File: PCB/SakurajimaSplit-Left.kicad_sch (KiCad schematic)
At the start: 49 parts, among them J1 Conn_01x01_Pin, J10 Conn_01x01_Pin, J11 Conn_01x01_Pin, J12 Conn_01x01_Pin, J13 Conn_01x01_Pin, J14 Conn_01x01_Pin, J15 Conn_01x01_Pin, J16 Conn_01x01_Pin, J17 Conn_01x01_Pin, J18 Conn_01x01_Pin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

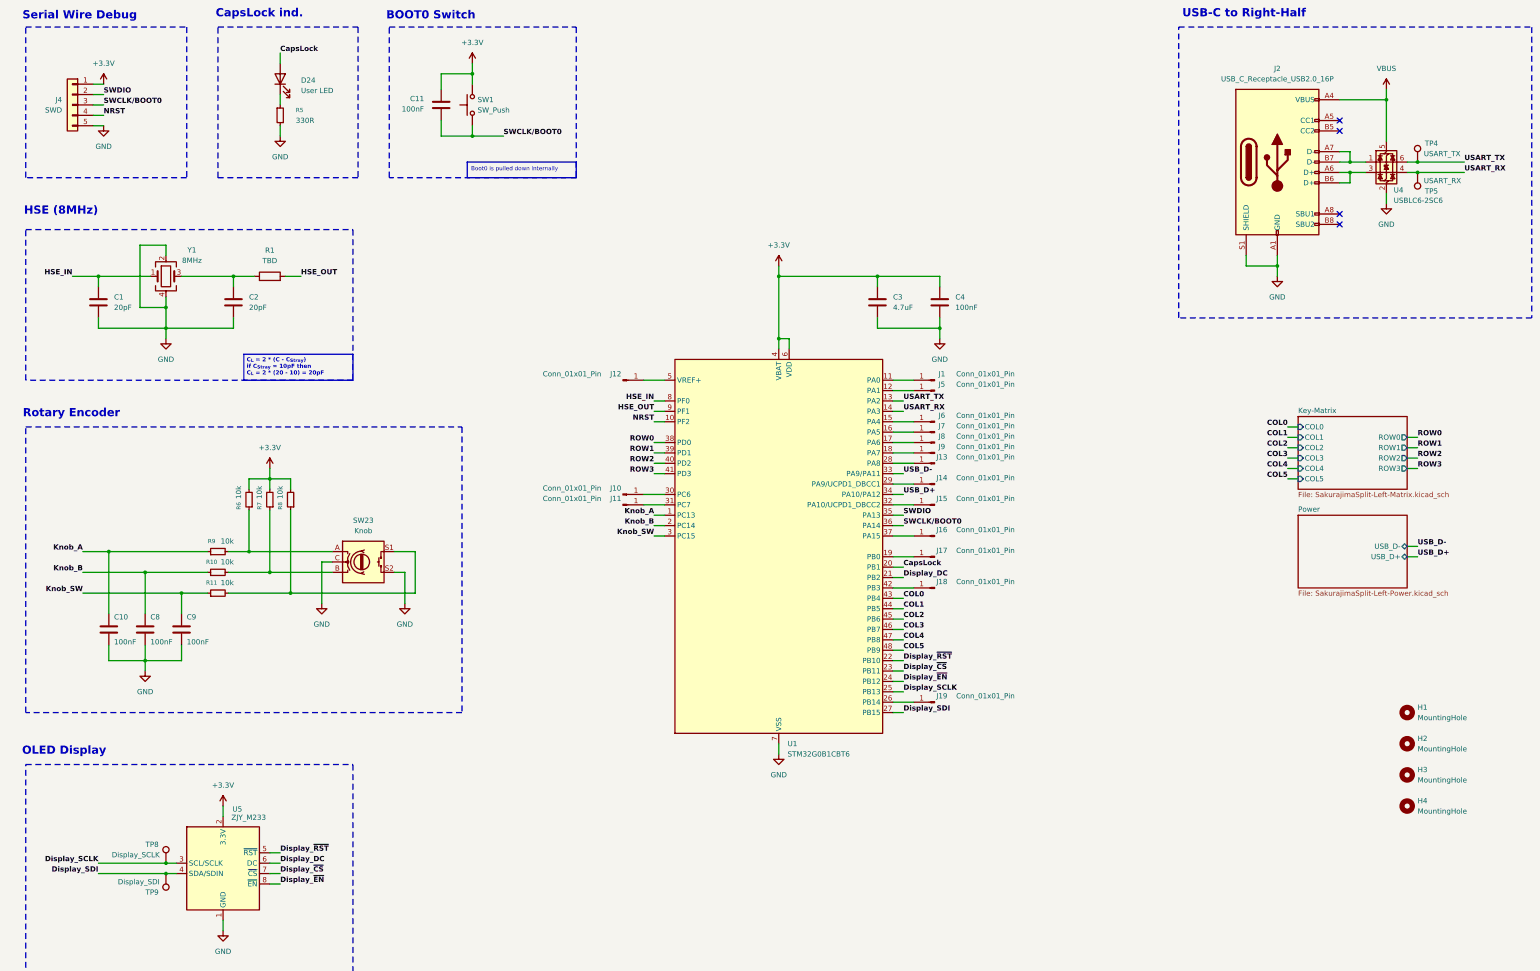
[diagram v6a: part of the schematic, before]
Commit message: feat(sch): cleanup and anotate schematic, choose components
- Fixed mistakes in schematic
- Anotated the schematic
- Found and chose components
- Added GND test points
- Ran ERC and fixed all errors and warnings
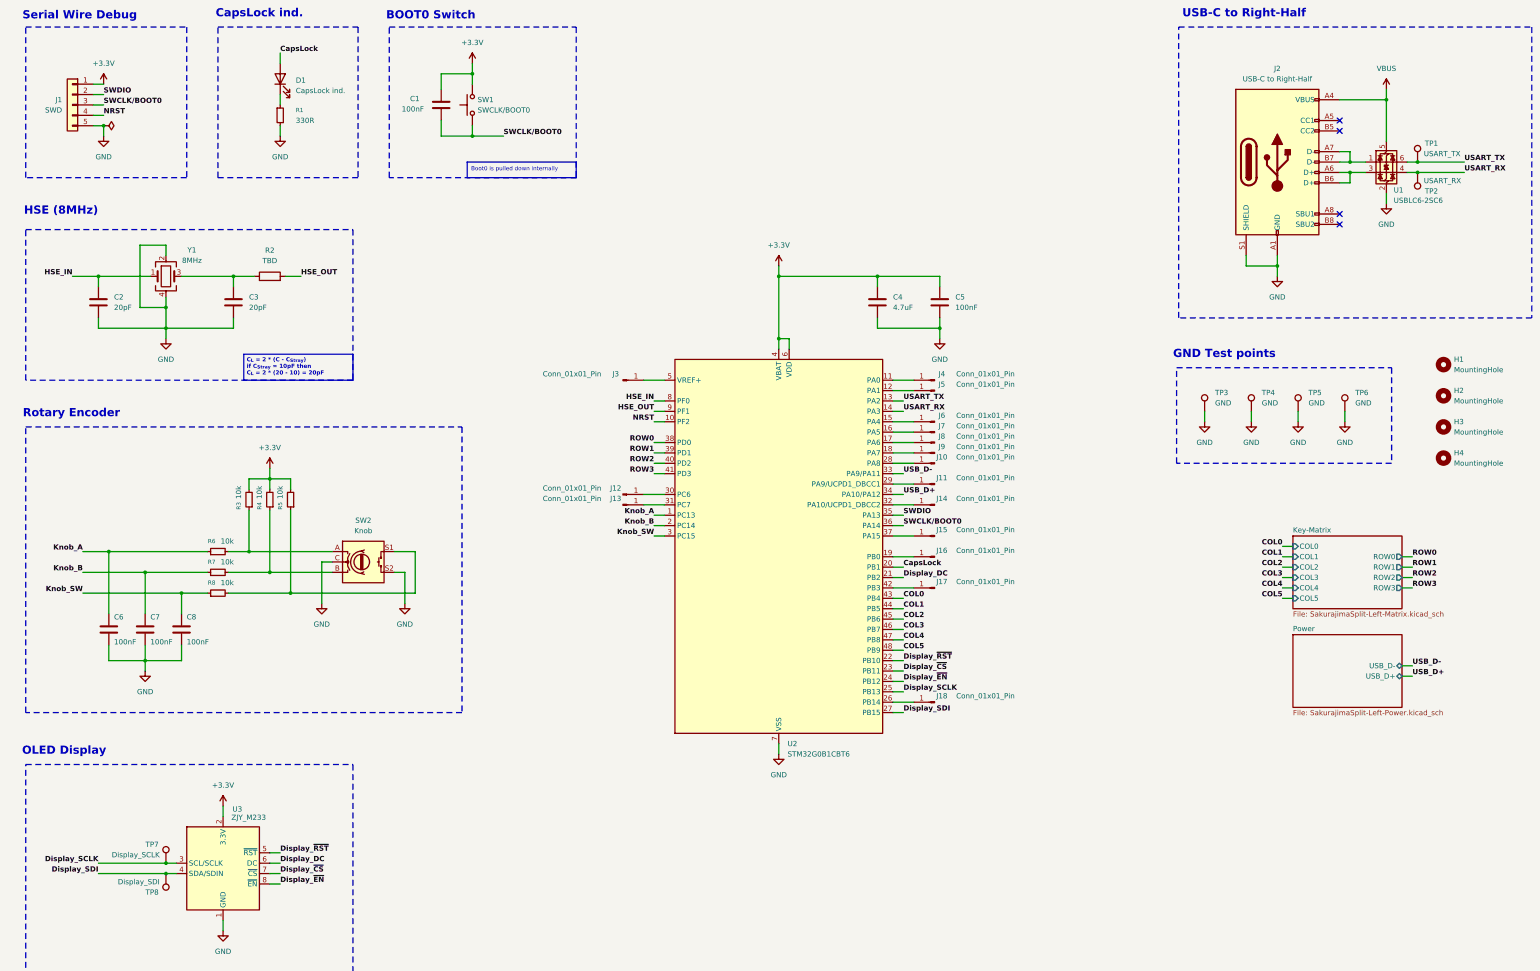
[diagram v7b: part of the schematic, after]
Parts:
- added TP3, TP4, TP5, TP6: GND, symbol Connector:TestPoint
- C1: renamed from C11; Distributor Link (none) -> https://lionelectronic.ir/products/4734-GRM188R72A104KA35D; Manufacturer (none) -> Murata; Manufacturer Part No. (none) -> GRM188R72A104KA35D
- C2: renamed from C1; Distributor Link (none) -> https://lionelectronic.ir/products/5170-GRM1555C1H220JA01D; Manufacturer (none) -> Murata; Manufacturer Part No. (none) -> GRM1555C1H220JA01D
- C3: renamed from C2; Distributor Link (none) -> https://lionelectronic.ir/products/5170-GRM1555C1H220JA01D; Manufacturer (none) -> Murata; Manufacturer Part No. (none) -> GRM1555C1H220JA01D
- C4: renamed from C3; Distributor Link (none) -> https://lionelectronic.ir/products/4714-GRM21BR61H475KE51L; Manufacturer (none) -> Murata; Manufacturer Part No. (none) -> GRM21BR61H475KE51L
- C5: renamed from C4; Distributor Link (none) -> https://lionelectronic.ir/products/4734-GRM188R72A104KA35D; Manufacturer (none) -> Murata; Manufacturer Part No. (none) -> GRM188R72A104KA35D
- C6: renamed from C10; Distributor Link (none) -> https://lionelectronic.ir/products/4734-GRM188R72A104KA35D; Manufacturer (none) -> Murata; Manufacturer Part No. (none) -> GRM188R72A104KA35D
- C7: renamed from C8; Distributor Link (none) -> https://lionelectronic.ir/products/4734-GRM188R72A104KA35D; Manufacturer (none) -> Murata; Manufacturer Part No. (none) -> GRM188R72A104KA35D
- C8: renamed from C9; Distributor Link (none) -> https://lionelectronic.ir/products/4734-GRM188R72A104KA35D; Manufacturer (none) -> Murata; Manufacturer Part No. (none) -> GRM188R72A104KA35D
- D1: renamed from D24; value User LED -> CapsLock ind.; Distributor Link (none) -> https://lionelectronic.ir/products/2215-XL-1608UWC-04; Manufacturer (none) -> XINGLIGHT; Manufacturer Part No. (none) -> XL-1608UWC-04
- H1, H2, H3, H4: Notes (none) -> M3 screws, Rubber o-rings
- J1: renamed from J4; Notes (none) -> 2.54mm right-angle pin header
- J10: renamed from J13; now left out of the parts list
- J11: renamed from J14; now left out of the parts list
- J12: renamed from J10; now left out of the parts list
- J13: renamed from J11; now left out of the parts list
- J14: renamed from J15; now left out of the parts list
- J15: renamed from J16; now left out of the parts list
- J16: renamed from J17; now left out of the parts list
- J17: renamed from J18; now left out of the parts list
- J18: renamed from J19; now left out of the parts list
- J2: value USB_C_Receptacle_USB2.0_16P -> USB-C to Right-Half; Distributor Link (none) -> https://lionelectronic.ir/products/3242-GT-USB-7010ASV; Manufacturer (none) -> G-Switch; Manufacturer Part No. (none) -> GT-USB-7010ASV
- J3: renamed from J12; now left out of the parts list
- J4: renamed from J1; now left out of the parts list
- J5, J6, J7, J8, J9: now left out of the parts list
- R1: renamed from R5; Distributor Link (none) -> https://lionelectronic.ir/products/1182-SER0603F330R; Manufacturer (none) -> VO Sub Brand (ER); Manufacturer Part No. (none) -> SER0603F330R
- R2: renamed from R1; Notes (none) -> Should be around 1k but 220R was also okay
- R3: renamed from R6; Distributor Link (none) -> https://lionelectronic.ir/products/1219-CR0603FA1002G; Manufacturer (none) -> LIZ Electronics; Manufacturer Part No. (none) -> CR0603FA1002G
- R4: renamed from R7; Distributor Link (none) -> https://lionelectronic.ir/products/1219-CR0603FA1002G; Manufacturer (none) -> LIZ Electronics; Manufacturer Part No. (none) -> CR0603FA1002G
- R5: renamed from R8; Distributor Link (none) -> https://lionelectronic.ir/products/1219-CR0603FA1002G; Manufacturer (none) -> LIZ Electronics; Manufacturer Part No. (none) -> CR0603FA1002G
- R6: renamed from R9; Distributor Link (none) -> https://lionelectronic.ir/products/1219-CR0603FA1002G; Manufacturer (none) -> LIZ Electronics; Manufacturer Part No. (none) -> CR0603FA1002G
- R7: renamed from R10; Distributor Link (none) -> https://lionelectronic.ir/products/1219-CR0603FA1002G; Manufacturer (none) -> LIZ Electronics; Manufacturer Part No. (none) -> CR0603FA1002G
- R8: renamed from R11; Distributor Link (none) -> https://lionelectronic.ir/products/1219-CR0603FA1002G; Manufacturer (none) -> LIZ Electronics; Manufacturer Part No. (none) -> CR0603FA1002G
- SW1: value SW_Push -> SWCLK/BOOT0; Distributor Link (none) -> https://lionelectronic.ir/products/5092-TS-1187A-B-A-B; Manufacturer (none) -> XKB Connection; Manufacturer Part No. (none) -> TS-1187A-B-A-B
- SW2: renamed from SW23; Distributor Link (none) -> https://lionelectronic.ir/products/2497-EC11L1525E05; Manufacturer (none) -> ALPSALPINE; Manufacturer Part No. (none) -> EC11L1525E05; Notes (none) -> Make sure height is okay
- TP1: renamed from TP4; now left out of the parts list
- TP2: renamed from TP5; now left out of the parts list
- TP7: renamed from TP8; now left out of the parts list
- TP8: renamed from TP9; now left out of the parts list
- U1: renamed from U4; Distributor Link (none) -> https://lionelectronic.ir/products/4780-USBLC6-4SC6; Manufacturer (none) -> STMicroelectronics; Manufacturer Part No. (none) -> USBLC6-4SC6
- U2: renamed from U1; Distributor Link (none) -> https://lionelectronic.ir/products/2851-STM32G0B1CBT6; Manufacturer (none) -> STMicroelectronics; Manufacturer Part No. (none) -> STM32G0B1CBT6
- U3: renamed from U5; Distributor Link (none) -> https://thecaferobot.com/store/2-23-inch-spi-iic-oled-displ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; Notes (none) -> Also need spacers
- Y1: Distributor Link (none) -> https://lionelectronic.ir/products/4281-X32258MSB4SI; Manufacturer (none) -> YXC; Manufacturer Part No. (none) -> X32258MSB4SI
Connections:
- net GND: now also TP3.1, TP4.1, TP5.1, TP6.1
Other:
- note added: "GND Test points"
- moved on the sheet: H1, H2, H3, H4

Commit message: feat(pcb): assign all footprints
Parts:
- C1, C5, C6, C7, C8: footprint (none) -> Capacitor_SMD:C_0603_1608Metric
- C2, C3: footprint (none) -> Capacitor_SMD:C_0402_1005Metric_Pad0.74x0.62mm_HandSolder
- C4: footprint (none) -> Capacitor_SMD:C_0805_2012Metric
- D1: footprint (none) -> LED_SMD:LED_0603_1608Metric
- H1, H2, H3, H4: footprint (none) -> MountingHole:MountingHole_3.2mm_M3_Pad
- J1: footprint (none) -> Connector_PinHeader_2.54mm:PinHeader_1x05_P2.54mm_Horizontal
- J10, J11, J12, J13, J14, J15, J16, J17, J18, J3, J4, J6, J7, J8, J9: footprint (none) -> Connector_Wire:SolderWirePad_1x01_SMD_1x2mm
- J2: footprint (none) -> Connector_USB:USB_C_Receptacle_G-Switch_GT-USB-7010ASV
- R1, R2, R3, R4, R5, R6, R7, R8: footprint (none) -> Resistor_SMD:R_0603_1608Metric
- SW1: footprint (none) -> Button_Switch_SMD:SW_Push_1P1T_XKB_TS-1187A
- SW2: footprint (none) -> Rotary_Encoder:RotaryEncoder_Alps_EC11E-Switch_Vertical_H20mm
- TP1, TP2, TP3, TP4, TP5, TP6, TP7, TP8: footprint (none) -> TestPoint:TestPoint_Pad_2.0x2.0mm
- Y1: footprint (none) -> Crystal:Crystal_SMD_3225-4Pin_3.2x2.5mm_HandSoldering
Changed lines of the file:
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@@
 			)
 		)
-		(property "Footprint" ""
+		(property "Footprint" "Rotary_Encoder:RotaryEncoder_Alps_EC11E-Switch_Vertical_H20mm"
 			(at 104.14 154.686 0)
 			(effects
@@
 			)
 		)
-		(property "Footprint" ""
+		(property "Footprint" "MountingHole:MountingHole_3.2mm_M3_Pad"
 			(at 372.11 118.11 0)
 			(effects
@@
 			)
 		)
-		(property "Footprint" ""
+		(property "Footprint" "Connector_Wire:SolderWirePad_1x01_SMD_1x2mm"
 			(at 247.65 165.1 0)
 			(effects
@@
 		(dnp no)
 		(fields_autoplaced yes)
-		(property "Reference" "#FLG04"
+		(property "Reference" "#FLG01"
 			(at 46.355 52.07 0)
 			(effects
@@
 			(project "SakurajimaSplit"
 				(path "/2049b6de-7453-46e1-ab60-70116abff9d6/d08add9a-e5d5-49be-809e-a90adb11436d"
-					(reference "#FLG04")
+					(reference "#FLG01")
 					(unit 1)
 				)
@@
 			)
 		)
-		(property "Footprint" ""
+		(property "Footprint" "Resistor_SMD:R_0603_1608Metric"
 			(at 72.39 161.29 0)
 			(effects
@@
 			)
 		)
-		(property "Footprint" ""
+		(property "Footprint" "Connector_Wire:SolderWirePad_1x01_SMD_1x2mm"
 			(at 247.65 157.48 0)
 			(effects
@@
 			)
 		)
-		(property "Footprint" ""
+		(property "Footprint" "Resistor_SMD:R_0603_1608Metric"
 			(at 72.39 156.21 0)
 			(effects
@@
 			)
 		)
-		(property "Footprint" ""
+		(property "Footprint" "Capacitor_SMD:C_0603_1608Metric"
 			(at 55.5752 179.07 0)
 			(effects
@@
 			)
 		)
-		(property "Footprint" ""
+		(property "Footprint" "Connector_Wire:SolderWirePad_1x01_SMD_1x2mm"
 			(at 171.45 142.24 0)
 			(effects
@@
 			)
 		)
-		(property "Footprint" ""
+		(property "Footprint" "Capacitor_SMD:C_0603_1608Metric"
 			(at 64.4652 179.07 0)
 			(effects
@@
 			)
 		)
-		(property "Footprint" ""
+		(property "Footprint" "Connector_Wire:SolderWirePad_1x01_SMD_1x2mm"
 			(at 247.65 129.54 0)
 			(effects
@@
 			)
 		)
-		(property "Footprint" ""
+		(property "Footprint" "Capacitor_SMD:C_0603_1608Metric"
 			(at 46.6852 179.07 0)
 			(effects
@@
 			)
 		)
-		(property "Footprint" ""
+		(property "Footprint" "TestPoint:TestPoint_Pad_2.0x2.0mm"
 			(at 370.84 60.96 0)
 			(effects
@@
 			)
 		)
-		(property "Footprint" ""
+		(property "Footprint" "Connector_Wire:SolderWirePad_1x01_SMD_1x2mm"
 			(at 247.65 139.7 0)
 			(effects
@@
 			)
 		)
-		(property "Footprint" ""
+		(property "Footprint" "Capacitor_SMD:C_0603_1608Metric"
 			(at 127.9652 50.8 0)
 			(effects
@@
 			)
 		)
-		(property "Footprint" ""
+		(property "Footprint" "Resistor_SMD:R_0603_1608Metric"
 			(at 90.17 143.51 0)
 			(effects
@@
 			)
 		)
-		(property "Footprint" ""
+		(property "Footprint" "Connector_Wire:SolderWirePad_1x01_SMD_1x2mm"
 			(at 247.65 193.04 0)
 			(effects
@@
 			)
 		)
-		(property "Footprint" ""
+		(property "Footprint" "Capacitor_SMD:C_0805_2012Metric"
 			(at 234.6452 99.06 0)
 			(effects
@@
 			)
 		)
-		(property "Footprint" ""
+		(property "Footprint" "Crystal:Crystal_SMD_3225-4Pin_3.2x2.5mm_HandSoldering"
 			(at 59.69 88.9 0)
 			(effects
@@
 			)
 		)
-		(property "Footprint" ""
+		(property "Footprint" "Capacitor_SMD:C_0603_1608Metric"
 			(at 249.8852 99.06 0)
 			(effects
@@
 			)
 		)
-		(property "Footprint" ""
+		(property "Footprint" "MountingHole:MountingHole_3.2mm_M3_Pad"
 			(at 372.11 110.49 0)
 			(effects
@@
 			)
 		)
-		(property "Footprint" ""
+		(property "Footprint" "Connector_Wire:SolderWirePad_1x01_SMD_1x2mm"
 			(at 247.65 124.46 0)
 			(effects
@@
 			)
 		)
-		(property "Footprint" ""
+		(property "Footprint" "Connector_Wire:SolderWirePad_1x01_SMD_1x2mm"
 			(at 171.45 144.78 0)
 			(effects
@@
 			)
 		)
-		(property "Footprint" ""
+		(property "Footprint" "TestPoint:TestPoint_Pad_2.0x2.0mm"
 			(at 318.77 121.92 0)
 			(effects
@@
 			)
 		)
-		(property "Footprint" ""
+		(property "Footprint" "Connector_PinHeader_2.54mm:PinHeader_1x05_P2.54mm_Horizontal"
 			(at 36.83 46.99 0)
 			(effects
@@
 			)
 		)
-		(property "Footprint" ""
+		(property "Footprint" "Capacitor_SMD:C_0402_1005Metric_Pad0.74x0.62mm_HandSolder"
 			(at 44.1452 99.06 0)
 			(effects
@@
 			)
 		)
-		(property "Footprint" ""
+		(property "Footprint" "Resistor_SMD:R_0603_1608Metric"
 			(at 85.09 90.678 90)
 			(effects
@@
 			)
 		)
-		(property "Footprint" ""
+		(property "Footprint" "Resistor_SMD:R_0603_1608Metric"
 			(at 80.01 143.51 0)
 			(effects
@@
 			)
 		)
-		(property "Footprint" ""
+		(property "Footprint" "Connector_Wire:SolderWirePad_1x01_SMD_1x2mm"
 			(at 247.65 114.3 0)
 			(effects
@@
 			)
 		)
-		(property "Footprint" ""
+		(property "Footprint" "Capacitor_SMD:C_0402_1005Metric_Pad0.74x0.62mm_HandSolder"
 			(at 77.1652 99.06 0)
 			(effects
@@
 			)
 		)
-		(property "Footprint" ""
+		(property "Footprint" "TestPoint:TestPoint_Pad_2.0x2.0mm"
 			(at 54.61 232.41 0)
 			(effects
@@
 			)
 		)
-		(property "Footprint" ""
+		(property "Footprint" "MountingHole:MountingHole_3.2mm_M3_Pad"
 			(at 372.11 125.73 0)
 			(effects
@@
 			)
 		)
-		(property "Footprint" ""
+		(property "Footprint" "Resistor_SMD:R_0603_1608Metric"
 			(at 85.09 143.51 0)
 			(effects
@@
 			)
 		)
-		(property "Footprint" ""
+		(property "Footprint" "LED_SMD:LED_0603_1608Metric"
 			(at 87.63 40.64 0)
 			(effects
@@
 			)
 		)
-		(property "Footprint" ""
+		(property "Footprint" "Connector_Wire:SolderWirePad_1x01_SMD_1x2mm"
 			(at 247.65 152.4 0)
 			(effects
@@
 			)
 		)
-		(property "Footprint" ""
+		(property "Footprint" "Button_Switch_SMD:SW_Push_1P1T_XKB_TS-1187A"
 			(at 129.54 46.99 0)
 			(effects
@@
 			)
 		)
-		(property "Footprint" ""
+		(property "Footprint" "Connector_Wire:SolderWirePad_1x01_SMD_1x2mm"
 			(at 247.65 134.62 0)
 			(effects
@@
 			)
 		)
-		(property "Footprint" ""
+		(property "Footprint" "Connector_Wire:SolderWirePad_1x01_SMD_1x2mm"
 			(at 247.65 144.78 0)
 			(effects
@@
 			)
 		)
-		(property "Footprint" ""
+		(property "Footprint" "TestPoint:TestPoint_Pad_2.0x2.0mm"
 			(at 54.61 234.95 0)
 			(effects
@@
 			)
 		)
-		(property "Footprint" ""
+		(property "Footprint" "Connector_Wire:SolderWirePad_1x01_SMD_1x2mm"
 			(at 247.65 132.08 0)
 			(effects
@@
 			)
 		)
-		(property "Footprint" ""
+		(property "Footprint" "Connector_Wire:SolderWirePad_1x01_SMD_1x2mm"
 			(at 247.65 127 0)
 			(effects
@@
 			)
 		)
-		(property "Footprint" ""
+		(property "Footprint" "Connector_Wire:SolderWirePad_1x01_SMD_1x2mm"
 			(at 171.45 114.3 0)
 			(effects
@@
 			)
 		)
-		(property "Footprint" ""
+		(property "Footprint" "Connector_USB:USB_C_Receptacle_G-Switch_GT-USB-7010ASV"
 			(at 335.28 60.96 0)
 			(effects
@@
 			)
 		)
-		(property "Footprint" ""
+		(property "Footprint" "TestPoint:TestPoint_Pad_2.0x2.0mm"
 			(at 353.06 121.92 0)
 			(effects
@@
 			)
 		)
-		(property "Footprint" ""
+		(property "Footprint" "TestPoint:TestPoint_Pad_2.0x2.0mm"
 			(at 370.84 63.5 0)
 			(effects
@@
 			)
 		)
-		(property "Footprint" ""
+		(property "Footprint" "MountingHole:MountingHole_3.2mm_M3_Pad"
 			(at 372.11 133.35 0)
 			(effects
@@
 			)
 		)
-		(property "Footprint" ""
+		(property "Footprint" "TestPoint:TestPoint_Pad_2.0x2.0mm"
 			(at 330.2 121.92 0)
 			(effects
@@
 			)
 		)
-		(property "Footprint" ""
+		(property "Footprint" "Resistor_SMD:R_0603_1608Metric"
 			(at 72.39 166.37 0)
 			(effects
@@
 			)
 		)
-		(property "Footprint" ""
+		(property "Footprint" "Resistor_SMD:R_0603_1608Metric"
 			(at 87.63 49.53 0)
 			(effects
@@
 			)
 		)
-		(property "Footprint" ""
+		(property "Footprint" "TestPoint:TestPoint_Pad_2.0x2.0mm"
 			(at 341.63 121.92 0)
 			(effects
